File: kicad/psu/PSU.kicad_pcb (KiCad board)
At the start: 2 copper layers, 54.5 x 54.5 mm, 44 parts, among them J1 B2B-PH-K-S, J2 Conn_01x08_Pin, U1 BQ21040DBVR, U2 RT4812GJ8F, U3 AP3445LW6-7, U4 AP3445LW6-7

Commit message: PSU Routing
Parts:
- added D2: D, Diode_SMD:D_0805_2012Metric, F.Cu at (160.0, 112.1)
- added D3: D, Diode_SMD:D_0805_2012Metric, F.Cu at (157.0, 112.1)
- added D4: D, Diode_SMD:D_0805_2012Metric, F.Cu at (153.5, 112.1)
- added D5: D, Diode_SMD:D_0805_2012Metric, F.Cu at (137.1, 112.2)
- moved R8 108.1 mm to (142.5, 108.0)
- moved R9 108.0 mm to (142.6, 111.0), turned to 180 degrees
- moved R11 101.2 mm to (150.4, 99.0), turned to 180 degrees
- moved R10 92.9 mm to (150.4, 96.0)
- moved L3 91.7 mm to (138.6, 104.5)
- moved C12 85.9 mm to (138.7, 99.5)
- moved R13 85.4 mm to (138.8, 96.4), turned to 180 degrees
- moved C10 84.8 mm to (132.0, 99.7)
- moved C9 79.5 mm to (132.0, 96.2)
- moved EN_1.8 78.8 mm to (156.2, 101.2), turned to 180 degrees
- moved EN_3.3 78.8 mm to (156.2, 97.5), turned to 180 degrees
- moved EN_5 78.7 mm to (156.2, 93.8), turned to 180 degrees
- moved R15 72.7 mm to (145.5, 96.5)
- moved C14 64.0 mm to (148.5, 106.5), turned to -90 degrees
- moved U4 60.9 mm to (145.2, 103.5)
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- renumbered JP3 to EN_1.8, JP2 to EN_3.3, JP1 to EN_5
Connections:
- F2 pad 2: +1.8V -> 1.8V
- F3 pad 2: +3.3V -> 3.3V
- F4 pad 2: +5V -> 5V
- J2 pad 1: 1.8V -> Net-(D2-K)
- J2 pad 2: 3.3V -> Net-(D3-K)
- J2 pad 3: 5V -> Net-(D4-K)
- J2 pad 5: PG_1.8 -> PG_3.3
- J2 pad 6: PG_3.3 -> PG_1.8
- J2 pad 8: Vcharger -> Net-(D5-A)
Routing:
- net Vbat: track 0.00 -> 127.8 mm
- net Vcharger: track 0.00 -> 53.2 mm, vias 0 -> 2
- net GND: track 0.00 -> 49.6 mm, vias 0 -> 19
- net Net-(C10-Pad2): track 0.00 -> 46.4 mm, vias 0 -> 8
- net Net-(U2-VOUT): track 0.00 -> 42.3 mm, vias 0 -> 2
- net PG_3.3: track 0.00 -> 35.0 mm, vias 0 -> 2
- net Net-(C11-Pad1): track 0.00 -> 23.0 mm
- net EN_5: track 0.00 -> 18.7 mm, vias 0 -> 4
- net Net-(EN_1.8-B): track 0.00 -> 17.5 mm
- net Net-(U3-FB): track 0.00 -> 17.0 mm
- net Net-(U2-FB): track 0.00 -> 16.9 mm
- net EN_1.8: track 0.00 -> 16.8 mm, vias 0 -> 6
- net Net-(U4-FB): track 0.00 -> 14.9 mm
- net EN_3.3: track 0.00 -> 14.1 mm, vias 0 -> 2
- net PG_1.8: track 0.00 -> 13.8 mm, vias 0 -> 2
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- added copper zone on B.Cu, net GND

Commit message: Added Test points and non fused 3.3V
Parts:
- added 1.8V1: TestPoint, TestPoint:TestPoint_Pad_1.5x1.5mm, F.Cu at (139.0, 108.0)
- added 3.3V1: TestPoint, TestPoint:TestPoint_Pad_1.5x1.5mm, F.Cu at (158.0, 104.0)
- added 5V1: TestPoint, TestPoint:TestPoint_Pad_1.5x1.5mm, F.Cu at (151.5, 91.0)
- added D6: D, Diode_SMD:D_0805_2012Metric, F.Cu at (159.0, 112.0)
- added GND1: TestPoint, TestPoint:TestPoint_Pad_1.5x1.5mm, F.Cu at (145.0, 72.0)
- F2, F3, F4: value 2A -> 1.5A
- J2: value Conn_01x08_Pin -> Conn_01x09_Pin; footprint Connector_PinHeader_2.54mm:PinHeader_1x08_P2.54mm_Vertical -> Connector_PinSocket_2.54mm:PinSocket_1x09_P2.54mm_Vertical
- moved J2 19.7 mm to (140.0, 116.0), turned to 90 degrees
- moved D2 1.50 mm to (161.5, 112.1)
- moved F2 1.50 mm to (161.5, 108.1)
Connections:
- net Net-(C10-Pad2) renamed 1.8V_T
- net Net-(C11-Pad1) renamed 3.3V_T
- net Net-(U2-VOUT) renamed 5V_T
- J1 pad 1: Net-(F1-Pad2) -> Vbat
- J2 pad 1: Net-(D2-K) -> Net-(D5-A)
- J2 pad 2: Net-(D3-K) -> Net-(J2-Pin_2)
- J2 pad 3: Net-(D4-K) -> PG_1.8
- J2 pad 4: GND -> PG_3.3
- J2 pad 5: PG_3.3 -> GND
- J2 pad 6: PG_1.8 -> Net-(D4-K)
- J2 pad 7: Net-(J2-Pin_7) -> Net-(D3-K)
- J2 pad 8: Net-(D5-A) -> Net-(D6-K)
- R8 pad 2: Net-(J2-Pin_7) -> Net-(J2-Pin_2)
- R9 pad 1: Net-(J2-Pin_7) -> Net-(J2-Pin_2)
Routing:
- net Net-(J2-Pin_2): track 0.00 -> 8.45 mm
- net Net-(J2-Pin_7): track 8.40 -> 0.00 mm
- net Net-(D6-K): track 0.00 -> 3.58 mm
- net 5V_T: track 42.3 -> 44.4 mm
- net 3.3V: track 2.14 -> 4.21 mm
- net GND: track 49.6 -> 51.6 mm, vias 19 -> 20
- net PG_3.3: track 35.0 -> 36.7 mm
- net 1.8V_T: track 46.4 -> 47.9 mm
- net PG_1.8: track 13.8 -> 14.6 mm
- net Net-(D5-A): track 5.41 -> 4.65 mm
- net Net-(D3-K): track 3.05 -> 3.73 mm

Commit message: PSU Rev 2
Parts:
- removed F1: 2A, Fuse:Fuse_0805_2012Metric
- added J3: *, PSAT_Library:GCT_USB4125-GF-A_REVA2, F.Cu at (177.6, 66.3)
- added R16: 22K, Resistor_SMD:R_0805_2012Metric, F.Cu at (184.2, 67.2)
- added R2: 1Meg, Resistor_SMD:R_0805_2012Metric, F.Cu at (204.3, 56.4)
- added R4: 1Meg, Resistor_SMD:R_0805_2012Metric, F.Cu at (201.6, 72.5)
- D2, D3, D4, D5, D6: value D -> D_Schottky
- moved R13 86.1 mm to (223.0, 78.3), turned to -90 degrees
- moved C9 83.9 mm to (212.6, 73.0), turned to -90 degrees
- moved C12 83.8 mm to (220.4, 80.7), turned to 90 degrees
- moved C10 82.5 mm to (210.2, 73.4), turned to -90 degrees
- moved L3 81.4 mm to (215.1, 76.5)
- moved R15 80.6 mm to (223.0, 74.5), turned to 90 degrees
- moved 1.8V1 80.0 mm to (213.7, 79.5), turned to 180 degrees
- moved U4 79.7 mm to (218.9, 73.0)
- moved C14 76.5 mm to (219.0, 76.9)
- moved 3.3V1 61.3 mm to (203.0, 62.4), turned to 180 degrees
- moved EN_3.3 61.0 mm to (203.0, 58.5), turned to 150 degrees
- moved D5 60.8 mm to (189.4, 81.1), turned to -90 degrees
- moved R11 60.7 mm to (196.2, 59.2), turned to 0 degrees
- moved R9 60.4 mm to (195.0, 80.9), turned to 90 degrees
- moved C7 60.1 mm to (208.3, 66.0)
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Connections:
- D3 pad 2: 3.3V -> 3.3V_T
- D4 pad 2: 5V -> 3.3V
- D6 pad 2: 3.3V -> 5V
- J2 pad 6: Net-(D4-K) -> Net-(D6-K)
- J2 pad 7: Net-(D3-K) -> Net-(D4-K)
- J2 pad 8: Net-(D6-K) -> Net-(D3-K)
- R11 pad 1: Net-(EN_1.8-B) -> EN_5
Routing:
- net GND: track 51.6 -> 79.5 mm, vias 20 -> 19
- net 1.8V_T: track 47.9 -> 22.0 mm, vias 8 -> 0
- net Vbat: track 127.8 -> 106.7 mm, vias 0 -> 12
- net Vcharger: track 53.2 -> 32.9 mm
- net PG_1.8: track 14.6 -> 32.4 mm, vias 2 -> 1
- net 3.3V_T: track 23.0 -> 35.4 mm
- net Net-(U2-FB): track 16.9 -> 5.36 mm
- net EN_5: track 18.7 -> 8.34 mm, vias 4 -> 0
- net Net-(U3-FB): track 17.0 -> 8.74 mm
- net EN_3.3: track 14.1 -> 6.41 mm, vias 2 -> 0
- net Net-(D1-K): track 6.80 -> 13.6 mm, vias 0 -> 2
- net 5V_T: track 44.4 -> 38.4 mm, vias 2 -> 4
- net Net-(F1-Pad2): track 5.77 -> 0.00 mm
- net Net-(U2-SW): track 6.55 -> 2.21 mm
- net Net-(U4-FB): track 14.9 -> 10.8 mm
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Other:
- board size 54.5 x 54.5 mm -> 54.5 x 47.7 mm

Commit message: Update PSU.kicad_pcb
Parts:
- moved J3 0.19 mm to (177.8, 66.4)
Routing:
- net 5V_T: track 38.4 -> 36.7 mm, vias 4 -> 2

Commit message: Minor PSU changes
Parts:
- added U5: LM66200DRLR, footprints:SOT-5X3_DRL_TEX, F.Cu at (192.0, 77.0)
- moved R1 4.44 mm to (193.0, 73.0), turned to 0 degrees
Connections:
- D5 pad 1: Vcharger -> Vcharger_MCU
- J3 pad A9: Vcharger -> Vcharger_USB
- J3 pad B9: Vcharger -> Vcharger_USB
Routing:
- net Vcharger_USB: track 0.00 -> 31.4 mm, vias 0 -> 3
- net Vcharger: track 32.9 -> 12.5 mm, vias 2 -> 0
- net GND: track 79.5 -> 89.3 mm, vias 19 -> 20
- net Vcharger_MCU: track 0.00 -> 6.44 mm
- net Vbat: track 106.7 -> 109.8 mm, vias 12 -> 10
- net 5V_T: track 36.7 -> 38.9 mm
- net Net-(U1-ISET): track 2.46 -> 4.19 mm

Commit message: PSU Diodes
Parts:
- D2, D3, D4, D5, D6: footprint Diode_SMD:D_0805_2012Metric -> Diode_SMD:D_SOD-123
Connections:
- U5 pad 8: Vcharger_USB -> unconnected-(U5-ST-Pad8)
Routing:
- net Vcharger_USB: track 31.4 -> 25.4 mm, vias 3 -> 2
- net 3.3V: track 3.82 -> 6.73 mm
- net 3.3V_T: track 35.4 -> 38.1 mm
- net Net-(D6-K): track 2.76 -> 2.05 mm
- net Net-(D3-K): track 2.75 -> 2.04 mm
- net Net-(D2-K): track 2.79 -> 2.08 mm
- net Net-(D5-A): track 2.60 -> 1.88 mm
- net 1.8V: track 1.77 -> 1.05 mm
- net Net-(D4-K): track 2.84 -> 2.13 mm
- net 5V: track 1.72 -> 1.01 mm

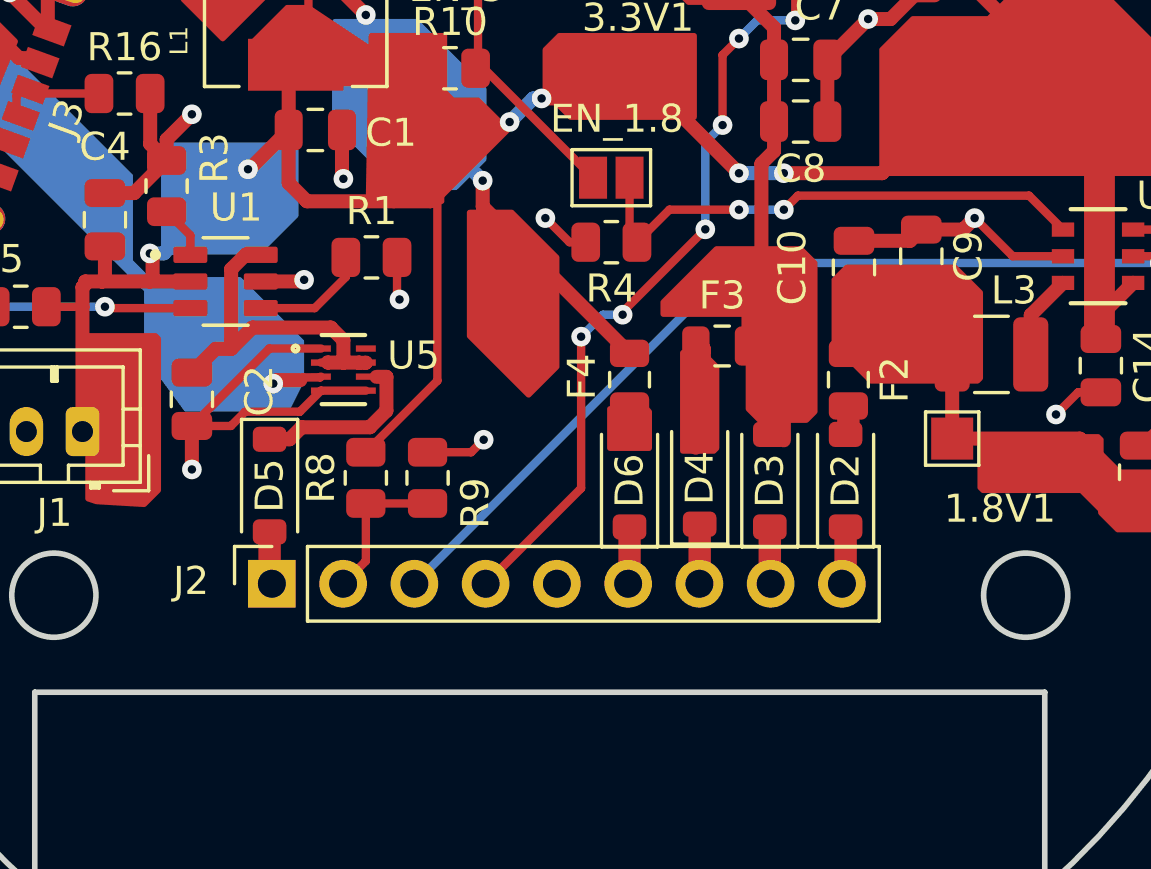
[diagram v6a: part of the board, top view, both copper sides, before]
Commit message: Minor PSU Tweaks
removed non existent resistors and updated components
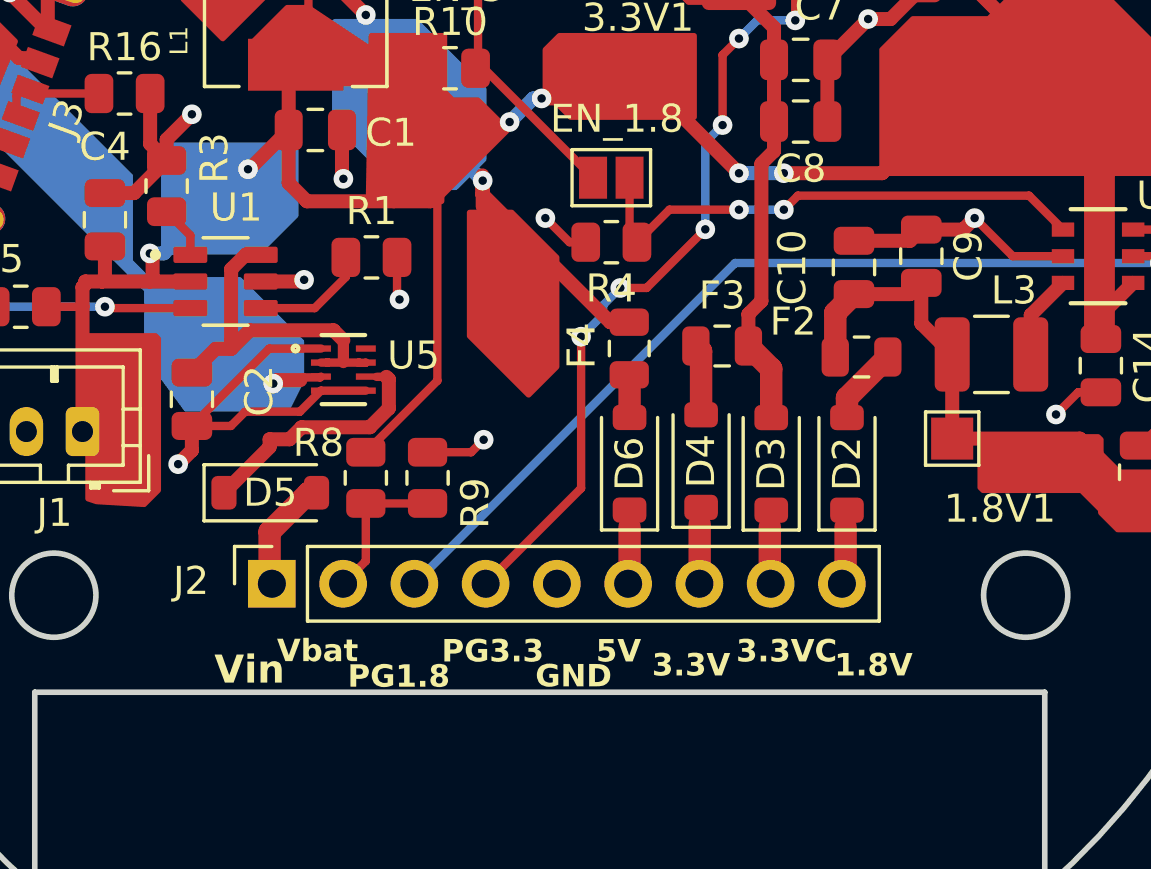
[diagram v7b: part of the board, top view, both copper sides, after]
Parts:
- moved F4 1.11 mm to (202.2, 76.2)
- moved F2 0.94 mm to (210.5, 76.5), turned to 0 degrees
- moved D6 0.60 mm to (202.2, 80.4)
- moved D3 0.60 mm to (207.2, 80.4)
- moved D4 0.60 mm to (204.8, 80.3)
- moved D2 0.60 mm to (209.9, 80.4)
- moved D5 0.26 mm to (189.4, 81.4), turned to 0 degrees
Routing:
- net 3.3V_T: track 38.1 -> 32.8 mm
- net 3.3V: track 6.73 -> 2.53 mm
- net Vcharger_MCU: track 6.15 -> 8.80 mm
- net Net-(D5-A): track 1.88 -> 4.13 mm
- net 1.8V: track 1.05 -> 2.76 mm
- net 1.8V_T: track 22.0 -> 22.6 mm
- net 5V: track 1.01 -> 1.53 mm
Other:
- board text added: "1.8V"
- board text added: "3.3V"
- board text added: "3.3VC"
- board text added: "5V"
- board text added: "GND"
- board text added: "PG1.8"
- board text added: "PG3.3"
- board text added: "Vbat"
- board text added: "Vin"

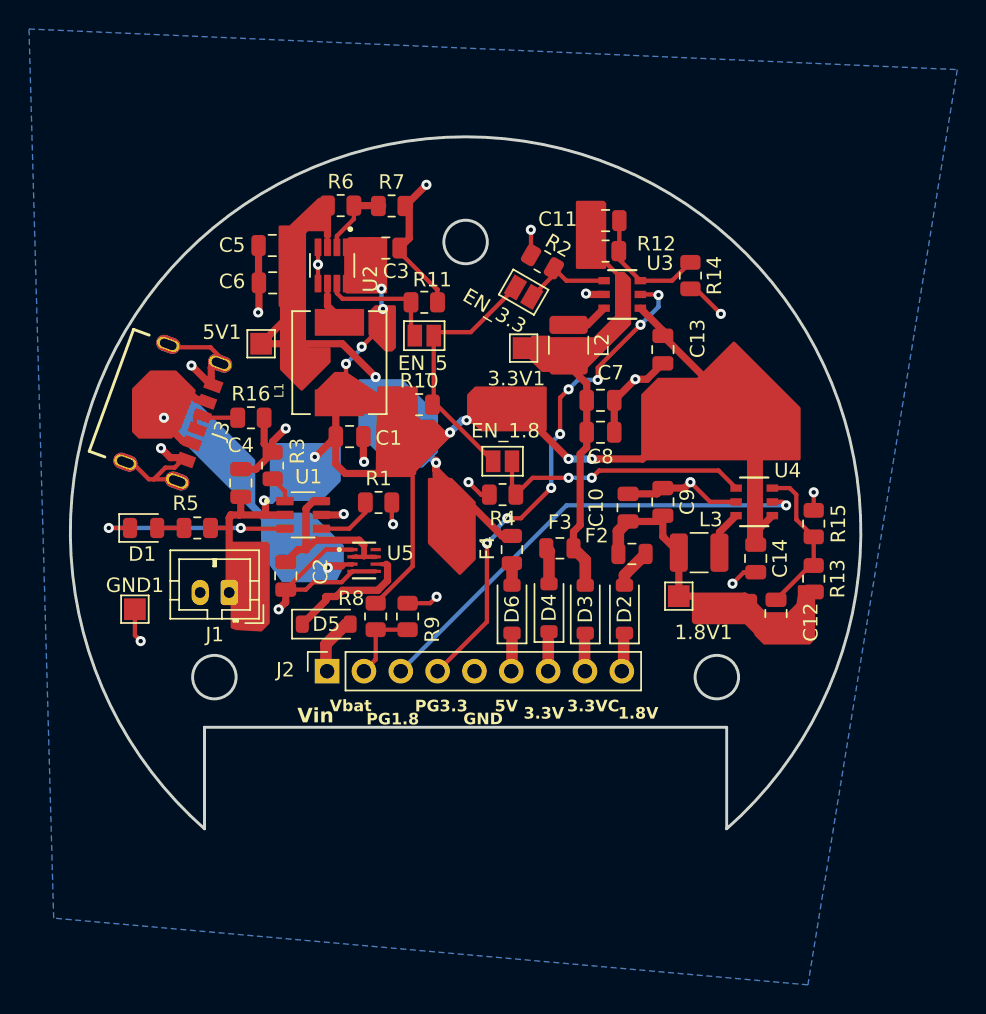
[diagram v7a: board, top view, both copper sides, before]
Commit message: new symbols & footprints for connectors and usb-c
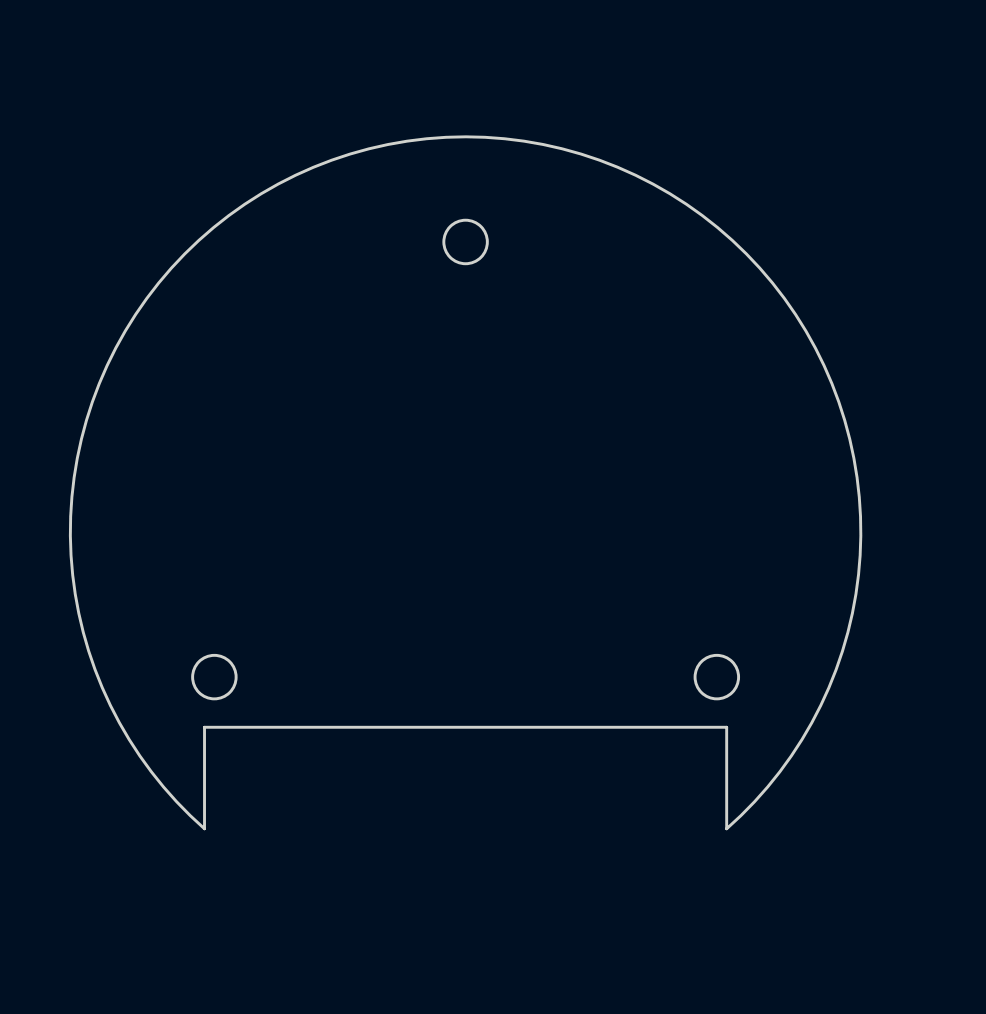
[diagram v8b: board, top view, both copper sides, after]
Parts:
- removed 1.8V1, 3.3V1, 5V1, GND1: TestPoint, TestPoint:TestPoint_Pad_1.5x1.5mm
- removed C1, C10, C13, C14, C3, C5, C6, C7, C8, C9: 22uF, Capacitor_SMD:C_0805_2012Metric
- removed C11, C12: 22pF, Capacitor_SMD:C_0805_2012Metric
- removed C2, C4: 2.2uF, Capacitor_SMD:C_0805_2012Metric
- removed D1: Green, LED_SMD:LED_0805_2012Metric
- removed D2, D3, D4, D5, D6: D_Schottky, Diode_SMD:D_SOD-123
- removed EN_1.8: EN_1.8, Jumper:SolderJumper-2_P1.3mm_Open_Pad1.0x1.5mm
- removed EN_3.3: EN_3.3, Jumper:SolderJumper-2_P1.3mm_Open_Pad1.0x1.5mm
- removed EN_5: EN_5, Jumper:SolderJumper-2_P1.3mm_Open_Pad1.0x1.5mm
- removed F2, F3, F4: 1.5A, Fuse:Fuse_0805_2012Metric
- removed J1: B2B-PH-K-S, Connector_JST:JST_PH_B2B-PH-K_1x02_P2.00mm_Vertical
- removed J2: Conn_01x09_Pin, Connector_PinSocket_2.54mm:PinSocket_1x09_P2.54mm_Vertical
- removed J3: *, PSAT_Library:GCT_USB4125-GF-A_REVA2
- removed L1: 1u5H, PSAT_Library:IND_SPM6530T-1R5M100
- removed L2, L3: 2u2H, Inductor_SMD:L_1210_3225Metric
- removed R1: 560, Resistor_SMD:R_0805_2012Metric
- removed R10: 1k5, Resistor_SMD:R_0805_2012Metric
- removed R11, R2, R4, R8, R9: 1Meg, Resistor_SMD:R_0805_2012Metric
- removed R12: 450K, Resistor_SMD:R_0805_2012Metric
- removed R13: 200K, Resistor_SMD:R_0805_2012Metric
- removed R14, R15, R6: 100K, Resistor_SMD:R_0805_2012Metric
- removed R16: 22K, Resistor_SMD:R_0805_2012Metric
- removed R3: 10K, Resistor_SMD:R_0805_2012Metric
- removed R5: 1K5, Resistor_SMD:R_0805_2012Metric
- removed R7: 900K, Resistor_SMD:R_0805_2012Metric
- removed U1: BQ21040DBVR, PSAT_Library:BQ21040DBVR
- removed U2: RT4812GJ8F, PSAT_Library:RT4812GJ8F
- removed U3, U4: AP3445LW6-7, PSAT_Library:SOT26_AP3445_DIO-L
- removed U5: LM66200DRLR, footprints:SOT-5X3_DRL_TEX
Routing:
- net Vbat: track 109.8 -> 0.00 mm, vias 10 -> 0
- net GND: track 89.3 -> 0.00 mm, vias 20 -> 0
- net 5V_T: track 39.3 -> 0.00 mm, vias 2 -> 0
- net PG_3.3: track 34.9 -> 0.00 mm, vias 8 -> 0
- net 3.3V_T: track 32.8 -> 0.00 mm
- net PG_1.8: track 32.4 -> 0.00 mm, vias 1 -> 0
- net Vcharger_USB: track 25.4 -> 0.00 mm, vias 2 -> 0
- net 1.8V_T: track 22.6 -> 0.00 mm
- net EN_1.8: track 18.8 -> 0.00 mm, vias 2 -> 0
- net Net-(EN_1.8-B): track 17.8 -> 0.00 mm
- net Net-(D1-K): track 13.6 -> 0.00 mm, vias 2 -> 0
- net Vcharger: track 12.9 -> 0.00 mm
- net Net-(U4-FB): track 10.8 -> 0.00 mm
- net Vcharger_MCU: track 8.80 -> 0.00 mm
- net Net-(U3-FB): track 8.74 -> 0.00 mm
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- removed copper zone on B.Cu, net GND
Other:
- board text removed: "1.8V"
- board text removed: "3.3V"
- board text removed: "3.3VC"
- board text removed: "5V"
- board text removed: "GND"
- board text removed: "PG1.8"
- board text removed: "PG3.3"
- board text removed: "Vbat"
- board text removed: "Vin"
